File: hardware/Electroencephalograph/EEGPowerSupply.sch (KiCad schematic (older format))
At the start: 26 parts, among them U10 TPS60403, U7 LP5912-1.8DRVT, U8 LP5912-1.8DRVT, U9 LP5912-1.8DRVT

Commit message: further routing
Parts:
- added D38, D39: D_Schottky, Diode_SMD:D_0805_2012Metric, symbol Device:D_Schottky
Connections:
- net A_GND: now also D38.1 (K), D39.2 (A)
- net A_VDD: now also D39.1 (K)
- net A_VSS: now also D38.2 (A)
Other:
- moved on the sheet: C68, C69, TP12, TP13
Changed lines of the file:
@@
 L Device:C C?
 U 1 1 5E0C8079
-P 7400 4650
+P 7500 4650
 AR Path="/5DF4CFF8/5E0C8079" Ref="C?"  Part="1"
 AR Path="/5DF61103/5E0C8079" Ref="C?"  Part="1"
 AR Path="/5DFE0AD6/5E0C8079" Ref="C?"  Part="1"
 AR Path="/5E0992D6/5E0C8079" Ref="C68"  Part="1"
-F 0 "C68" H 7515 4696 50  0000 L CNN
-F 1 "1u" H 7515 4605 50  0000 L CNN
-F 2 "Capacitor_SMD:C_0402_1005Metric" H 7438 4500 50  0001 C CNN
-F 3 "~" H 7400 4650 50  0001 C CNN
-	1    7400 4650
-	1    0    0    -1
-$EndComp
-Wire Wire Line
-	7400 3850 7400 4500
-Wire Wire Line
-	7400 5500 7400 4800
+F 0 "C68" H 7615 4696 50  0000 L CNN
+F 1 "1u" H 7615 4605 50  0000 L CNN
+F 2 "Capacitor_SMD:C_0402_1005Metric" H 7538 4500 50  0001 C CNN
+F 3 "~" H 7500 4650 50  0001 C CNN
+	1    7500 4650
+	1    0    0    -1
+$EndComp
+Wire Wire Line
+	7500 3850 7500 4500
+Wire Wire Line
+	7500 5500 7500 4800
 $Comp
 L Device:C C?
 U 1 1 5E0C9776
-P 7850 4650
+P 7950 4650
 AR Path="/5DF4CFF8/5E0C9776" Ref="C?"  Part="1"
 AR Path="/5DF61103/5E0C9776" Ref="C?"  Part="1"
 AR Path="/5DFE0AD6/5E0C9776" Ref="C?"  Part="1"
 AR Path="/5E0992D6/5E0C9776" Ref="C69"  Part="1"
-F 0 "C69" H 7965 4696 50  0000 L CNN
-F 1 "100n" H 7965 4605 50  0000 L CNN
-F 2 "Capacitor_SMD:C_0402_1005Metric" H 7888 4500 50  0001 C CNN
-F 3 "~" H 7850 4650 50  0001 C CNN
-	1    7850 4650
+F 0 "C69" H 8065 4696 50  0000 L CNN
+F 1 "100n" H 8065 4605 50  0000 L CNN
+F 2 "Capacitor_SMD:C_0402_1005Metric" H 7988 4500 50  0001 C CNN
+F 3 "~" H 7950 4650 50  0001 C CNN
+	1    7950 4650
 	1    0    0    -1
 $EndComp
 Connection ~ 6500 3850
 Wire Wire Line
-	7400 3850 7850 3850
-Wire Wire Line
-	7850 3850 7850 4500
-Connection ~ 7400 3850
-Wire Wire Line
-	7400 5500 7850 5500
-Wire Wire Line
-	7850 5500 7850 4800
-Connection ~ 7400 5500
+	7500 3850 7950 3850
+Wire Wire Line
+	7950 3850 7950 4500
+Connection ~ 7500 3850
+Wire Wire Line
+	7500 5500 7950 5500
+Wire Wire Line
+	7950 5500 7950 4800
+Connection ~ 7500 5500
 $Comp
 L Electroencephalograph:A_VDD #PWR125
 U 1 1 5E0E8DCD
-P 8150 3750
-F 0 "#PWR125" H 8150 3850 50  0001 C CNN
-F 1 "A_VDD" H 8167 3923 50  0000 C CNN
-F 2 "" H 8150 3850 50  0001 C CNN
-F 3 "" H 8150 3850 50  0001 C CNN
-	1    8150 3750
+P 8250 3750
+F 0 "#PWR125" H 8250 3850 50  0001 C CNN
+F 1 "A_VDD" H 8267 3923 50  0000 C CNN
+F 2 "" H 8250 3850 50  0001 C CNN
+F 3 "" H 8250 3850 50  0001 C CNN
+	1    8250 3750
 	1    0    0    -1
 $EndComp
@@
 L Electroencephalograph:A_VSS #PWR126
 U 1 1 5E0E9936
-P 8150 5550
-F 0 "#PWR126" H 8150 5550 50  0001 C CNN
-F 1 "A_VSS" H 8168 5723 50  0000 C CNN
-F 2 "" H 8150 5550 50  0001 C CNN
-F 3 "" H 8150 5550 50  0001 C CNN
-	1    8150 5550
+P 8250 5550
+F 0 "#PWR126" H 8250 5550 50  0001 C CNN
+F 1 "A_VSS" H 8268 5723 50  0000 C CNN
+F 2 "" H 8250 5550 50  0001 C CNN
+F 3 "" H 8250 5550 50  0001 C CNN
+	1    8250 5550
 	-1   0    0    1
 $EndComp
@@
 $EndComp
 Wire Wire Line
-	7850 5500 8150 5500
-Wire Wire Line
-	8150 5500 8150 5550
-Connection ~ 7850 5500
-Wire Wire Line
-	7850 3850 8150 3850
-Connection ~ 7850 3850
-Wire Wire Line
-	8150 3750 8150 3850
+	7950 5500 8250 5500
+Wire Wire Line
+	8250 5500 8250 5550
+Connection ~ 7950 5500
+Wire Wire Line
+	7950 3850 8250 3850
+Connection ~ 7950 3850
+Wire Wire Line
+	8250 3750 8250 3850
 Wire Wire Line
 	5550 2500 5450 2500
@@
 L Connector:TestPoint TP?
 U 1 1 5E1A0405
-P 7400 3800
+P 7500 3800
 AR Path="/5DF61103/5E1A0405" Ref="TP?"  Part="1"
 AR Path="/5E0992D6/5E1A0405" Ref="TP12"  Part="1"
-F 0 "TP12" H 7458 3918 50  0000 L CNN
-F 1 "TestPoint" H 7458 3827 50  0000 L CNN
-F 2 "TestPoint:TestPoint_Pad_1.5x1.5mm" H 7600 3800 50  0001 C CNN
-F 3 "~" H 7600 3800 50  0001 C CNN
-	1    7400 3800
+F 0 "TP12" H 7558 3918 50  0000 L CNN
+F 1 "TestPoint" H 7558 3827 50  0000 L CNN
+F 2 "TestPoint:TestPoint_Pad_1.5x1.5mm" H 7700 3800 50  0001 C CNN
+F 3 "~" H 7700 3800 50  0001 C CNN
+	1    7500 3800
 	1    0    0    -1
 $EndComp
@@
 L Connector:TestPoint TP?
 U 1 1 5E1A2E89
-P 7400 5600
+P 7500 5600
 AR Path="/5DF61103/5E1A2E89" Ref="TP?"  Part="1"
 AR Path="/5E0992D6/5E1A2E89" Ref="TP13"  Part="1"
-F 0 "TP13" H 7342 5626 50  0000 R CNN
-F 1 "TestPoint" H 7342 5717 50  0000 R CNN
-F 2 "TestPoint:TestPoint_Pad_1.5x1.5mm" H 7600 5600 50  0001 C CNN
-F 3 "~" H 7600 5600 50  0001 C CNN
-	1    7400 5600
+F 0 "TP13" H 7442 5626 50  0000 R CNN
+F 1 "TestPoint" H 7442 5717 50  0000 R CNN
+F 2 "TestPoint:TestPoint_Pad_1.5x1.5mm" H 7700 5600 50  0001 C CNN
+F 3 "~" H 7700 5600 50  0001 C CNN
+	1    7500 5600
 	-1   0    0    1
 $EndComp
 Wire Wire Line
-	7400 3800 7400 3850
-Wire Wire Line
-	7400 5600 7400 5500
+	7500 3800 7500 3850
+Wire Wire Line
+	7500 5600 7500 5500
 $Comp
 L Connector:TestPoint TP?
@@
 Connection ~ 7050 2400
 Wire Wire Line
-	7050 2400 8250 2400
-Wire Wire Line
 	7050 2300 7050 2400
 Wire Wire Line
@@
 Connection ~ 6500 5500
 Wire Wire Line
-	6500 5500 7400 5500
-Wire Wire Line
-	6500 3850 7400 3850
+	6500 5500 6950 5500
+Wire Wire Line
+	6500 3850 7000 3850
 Text Notes 4800 6000 0    59   ~ 12
 TODO: change regulator to one that accepts negative voltages
@@
 	1    0    0    1
 $EndComp
+$Comp
+L Electroencephalograph:A_GND #PWR?
+U 1 1 5E2683D7
+P 7000 4400
+AR Path="/5DFE0AD6/5E2683D7" Ref="#PWR?"  Part="1"
+AR Path="/5E0992D6/5E2683D7" Ref="#PWR205"  Part="1"
+F 0 "#PWR205" H 7000 4425 50  0001 C CNN
+F 1 "A_GND" H 7017 4227 50  0000 C CNN
+F 2 "" H 7000 4425 50  0001 C CNN
+F 3 "" H 7000 4425 50  0001 C CNN
+	1    7000 4400
+	1    0    0    -1
+$EndComp
+$Comp
+L Electroencephalograph:A_GND #PWR?
+U 1 1 5E26AFDA
+P 6950 5000
+AR Path="/5DFE0AD6/5E26AFDA" Ref="#PWR?"  Part="1"
+AR Path="/5E0992D6/5E26AFDA" Ref="#PWR204"  Part="1"
+F 0 "#PWR204" H 6950 5025 50  0001 C CNN
+F 1 "A_GND" H 6967 4827 50  0000 C CNN
+F 2 "" H 6950 5025 50  0001 C CNN
+F 3 "" H 6950 5025 50  0001 C CNN
+	1    6950 5000
+	1    0    0    1
+$EndComp
+Wire Wire Line
+	7000 3950 7000 3850
+Connection ~ 7000 3850
+Wire Wire Line
+	7000 3850 7500 3850
+Wire Wire Line
+	6950 5400 6950 5500
+Connection ~ 6950 5500
+Wire Wire Line
+	6950 5500 7500 5500
+Wire Wire Line
+	6950 5100 6950 5000
+Wire Wire Line
+	7000 4400 7000 4250
+Wire Wire Line
+	7050 2400 8250 2400
+$Comp
+L Device:D_Schottky D38
+U 1 1 5E289000
+P 6950 5250
+F 0 "D38" V 6904 5329 50  0000 L CNN
+F 1 "D_Schottky" V 6995 5329 50  0000 L CNN
+F 2 "Diode_SMD:D_0805_2012Metric" H 6950 5250 50  0001 C CNN
+F 3 "~" H 6950 5250 50  0001 C CNN
+	1    6950 5250
+	0    1    1    0
+$EndComp
+$Comp
+L Device:D_Schottky D39
+U 1 1 5E28D2A7
+P 7000 4100
+F 0 "D39" V 6954 4179 50  0000 L CNN
+F 1 "D_Schottky" V 7045 4179 50  0000 L CNN
+F 2 "Diode_SMD:D_0805_2012Metric" H 7000 4100 50  0001 C CNN
+F 3 "~" H 7000 4100 50  0001 C CNN
+	1    7000 4100
+	0    1    1    0
+$EndComp
 $EndSCHEMATC

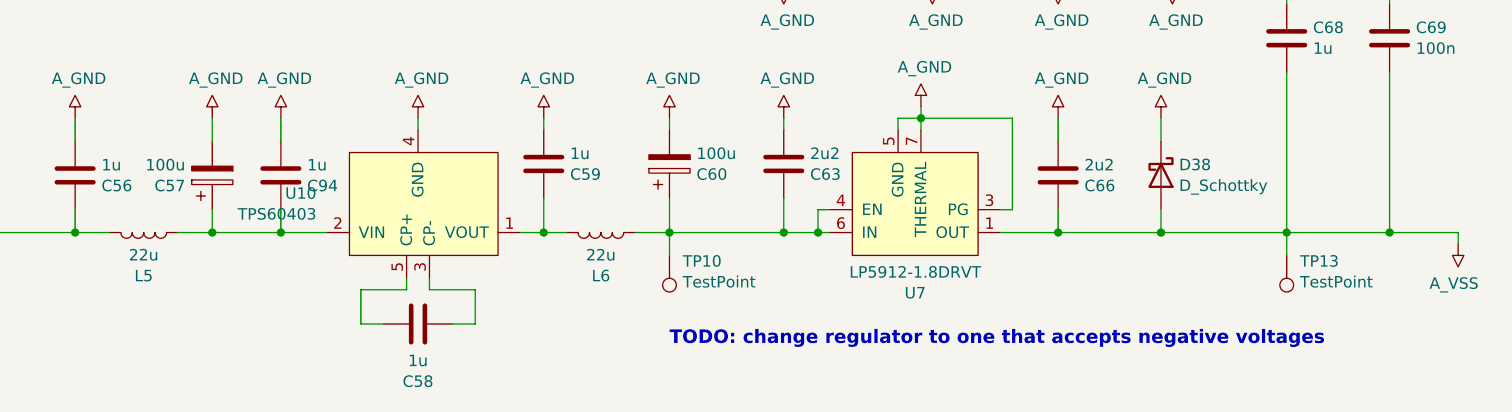
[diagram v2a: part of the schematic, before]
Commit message: fix #41, fix #18
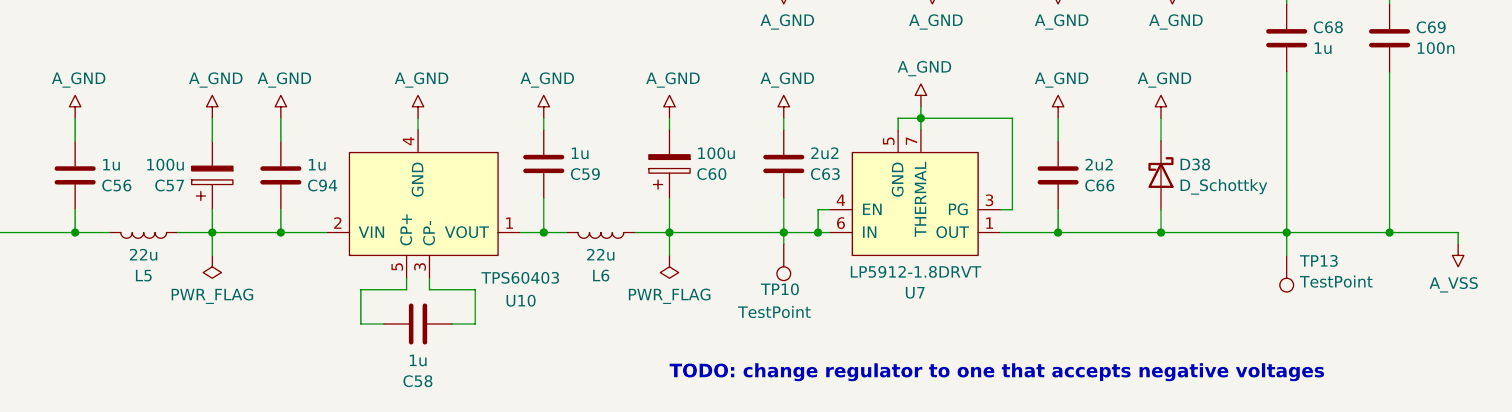
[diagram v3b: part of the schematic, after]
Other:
- moved on the sheet: TP10
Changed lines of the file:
@@
 $Descr A4 11693 8268
 encoding utf-8
-Sheet 6 8
+Sheet 6 9
 Title "EEG power supply"
 Date ""
@@
 L Connector:TestPoint TP?
 U 1 1 5E1AE8F5
-P 4800 5600
+P 5300 5550
 AR Path="/5DF61103/5E1AE8F5" Ref="TP?"  Part="1"
 AR Path="/5E0992D6/5E1AE8F5" Ref="TP10"  Part="1"
-F 0 "TP10" H 4742 5626 50  0000 R CNN
-F 1 "TestPoint" H 4742 5717 50  0000 R CNN
-F 2 "TestPoint:TestPoint_Pad_1.5x1.5mm" H 5000 5600 50  0001 C CNN
-F 3 "~" H 5000 5600 50  0001 C CNN
-	1    4800 5600
+F 0 "TP10" H 5400 5750 50  0000 R CNN
+F 1 "TestPoint" H 5500 5850 50  0000 R CNN
+F 2 "TestPoint:TestPoint_Pad_1.5x1.5mm" H 5500 5550 50  0001 C CNN
+F 3 "~" H 5500 5550 50  0001 C CNN
+	1    5300 5550
 	-1   0    0    1
 $EndComp
-Wire Wire Line
-	4800 5600 4800 5500
 $Comp
 L Device:L L?
@@
 Wire Wire Line
 	6500 3850 7000 3850
-Text Notes 4800 6000 0    59   ~ 12
+Text Notes 4800 6150 0    59   ~ 12
 TODO: change regulator to one that accepts negative voltages
 Wire Wire Line
@@
 U 1 1 5E0F81A7
 P 3700 5400
-F 0 "U10" H 3256 5329 50  0000 R CNN
-F 1 "TPS60403" H 3256 5420 50  0000 R CNN
+F 0 "U10" H 4150 5800 50  0000 C CNN
+F 1 "TPS60403" H 4150 5700 50  0000 C CNN
 F 2 "Package_TO_SOT_SMD:SOT-23-5" H 4150 5700 50  0001 C CNN
 F 3 "http://www.ti.com/lit/ds/symlink/tps60402.pdf" H 4150 5700 50  0001 C CNN
@@
 	0    1    1    0
 $EndComp
+Wire Wire Line
+	5300 5550 5300 5500
+$Comp
+L power:PWR_FLAG #FLG0102
+U 1 1 5ECFE874
+P 4800 5600
+F 0 "#FLG0102" H 4800 5675 50  0001 C CNN
+F 1 "PWR_FLAG" H 4800 5773 50  0000 C CNN
+F 2 "" H 4800 5600 50  0001 C CNN
+F 3 "~" H 4800 5600 50  0001 C CNN
+	1    4800 5600
+	-1   0    0    1
+$EndComp
+$Comp
+L power:PWR_FLAG #FLG0103
+U 1 1 5ED23C84
+P 2800 5600
+F 0 "#FLG0103" H 2800 5675 50  0001 C CNN
+F 1 "PWR_FLAG" H 2800 5773 50  0000 C CNN
+F 2 "" H 2800 5600 50  0001 C CNN
+F 3 "~" H 2800 5600 50  0001 C CNN
+	1    2800 5600
+	-1   0    0    1
+$EndComp
+Wire Wire Line
+	2800 5600 2800 5500
+Wire Wire Line
+	4800 5500 4800 5600
 $EndSCHEMATC
